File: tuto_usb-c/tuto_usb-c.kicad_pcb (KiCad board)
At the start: 4 copper layers, 50 x 40 mm, 38 parts, among them J1 USB_C_Receptacle_USB2.0, J2 Conn_01x06, J301 Conn_ST_STDC14, J4 Conn_01x06, U1 USBLC6-2SC6, U2 MCP1802x-xx02xOT, U3 STM32G431KBT6, Y1 Crystal_GND24_Small

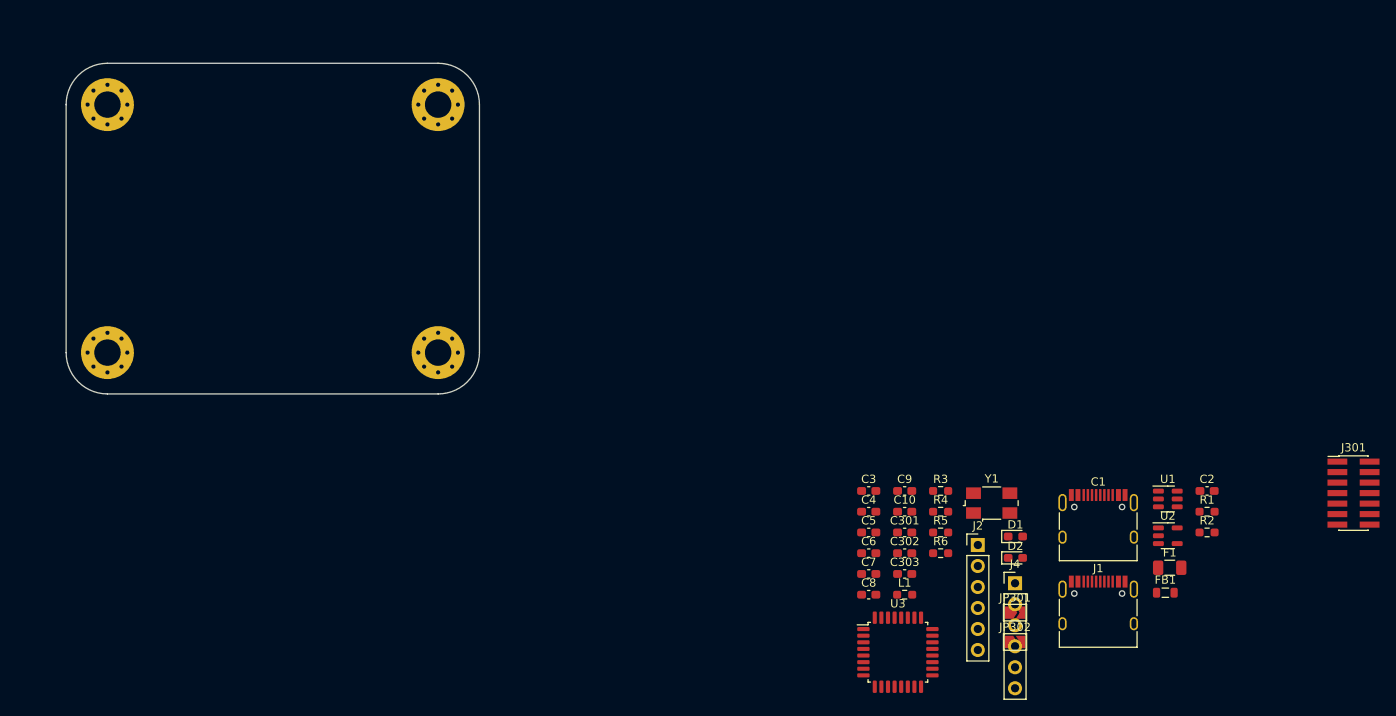
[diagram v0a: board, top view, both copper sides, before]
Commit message: modif routing - add gng plane
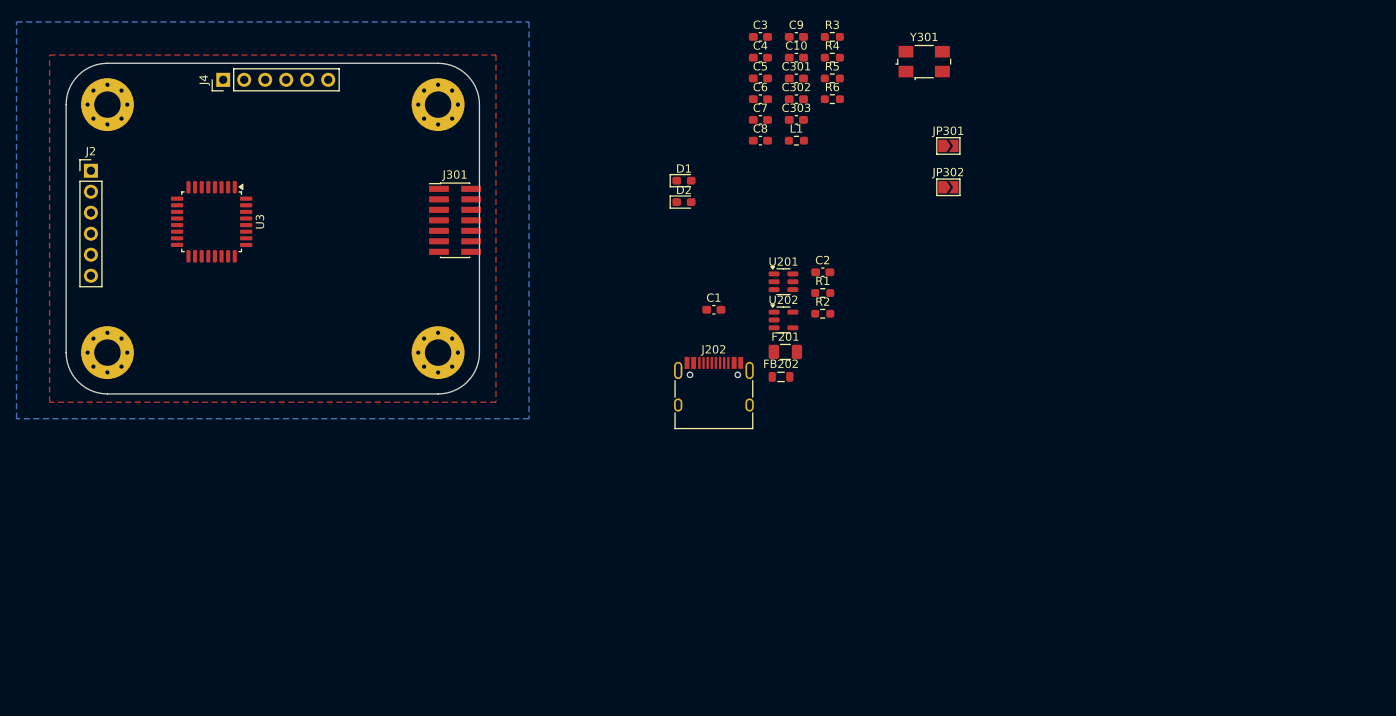
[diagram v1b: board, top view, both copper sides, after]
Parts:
- removed F1: 250mA, Fuse:Fuse_1206_3216Metric
- removed FB1: 600 @ 100MHz, Inductor_SMD:L_0805_2012Metric
- removed J1: USB_C_Receptacle_USB2.0, Connector_USB:USB_C_Receptacle_HRO_TYPE-C-31-M-12
- removed U1: USBLC6-2SC6, Package_TO_SOT_SMD:SOT-23-6
- removed U2: MCP1802x-xx02xOT, Package_TO_SOT_SMD:SOT-23-5
- removed Y1: Crystal_GND24_Small, Crystal:Crystal_SMD_0603-4Pin_6.0x3.5mm
- added F201: 250mA, Fuse:Fuse_1206_3216Metric, F.Cu at (182.0, 79.9)
- added FB202: 600 @ 100MHz, Inductor_SMD:L_0805_2012Metric, F.Cu at (181.5, 82.9)
- added J202: USB_C_Receptacle_USB2.0_16P, Connector_USB:USB_C_Receptacle_HRO_TYPE-C-31-M-12, F.Cu at (173.4, 85.3)
- added U201: USBLC6-2SC6, Package_TO_SOT_SMD:SOT-23-6, F.Cu at (181.8, 71.4)
- added U202: MCP1802x-xx02xOT, Package_TO_SOT_SMD:SOT-23-5, F.Cu at (181.8, 76.0)
- added Y301: Crystal_GND24_Small, Crystal:Crystal_SMD_0603-4Pin_6.0x3.5mm, F.Cu at (198.8, 44.8)
- C1: footprint Connector_USB:USB_C_Receptacle_HRO_TYPE-C-31-M-12 -> Capacitor_SMD:C_0603_1608Metric_Pad1.08x0.95mm_HandSolder
- moved J2 116.5 mm to (98.0, 58.0)
- moved J301 113.6 mm to (142.1, 64.0)
- moved J4 113.5 mm to (114.0, 47.0), turned to 90 degrees
- moved U3 98.0 mm to (112.6, 64.2), turned to -90 degrees
- moved D1 58.8 mm to (169.7, 59.2)
- moved D2 58.8 mm to (169.7, 61.8)
- moved JP301 57.0 mm to (201.7, 55.0)
- moved C10 56.5 mm to (183.3, 44.3)
- moved C303 56.5 mm to (183.3, 51.9)
- moved C4 56.5 mm to (179.0, 44.3)
- moved C7 56.5 mm to (179.0, 51.9)
- moved R4 56.5 mm to (187.7, 44.3)
- moved C3 56.5 mm to (179.0, 41.8)
- moved C301 56.5 mm to (183.3, 46.8)
- moved C302 56.5 mm to (183.3, 49.3)
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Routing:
- added copper zone on In2.Cu, net +3.3V
- added copper zone on B.Cu, net GND
- added copper zone on F.Cu, net GND
- added copper zone on In1.Cu, net GND

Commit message: placement des composants sur la  PCB
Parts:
- Y301: footprint Crystal:Crystal_SMD_0603-4Pin_6.0x3.5mm -> Crystal:Crystal_SMD_EuroQuartz_MT-4Pin_3.2x2.5mm
- moved Y301 97.7 mm to (102.8, 63.4), turned to 90 degrees
- moved JP302 87.9 mm to (114.7, 47.7)
- moved JP301 87.1 mm to (114.7, 51.6), turned to 180 degrees
- moved R4 83.8 mm to (106.3, 64.5)
- moved C5 78.6 mm to (102.8, 66.2), turned to 180 degrees
- moved R6 78.0 mm to (109.9, 54.6), turned to 90 degrees
- moved C4 77.9 mm to (102.8, 60.6), turned to 180 degrees
- moved C9 76.3 mm to (107.4, 49.6), turned to 90 degrees
- moved R5 76.0 mm to (112.1, 54.6), turned to 90 degrees
- moved C10 74.5 mm to (109.0, 49.6), turned to 90 degrees
- moved R3 73.8 mm to (116.8, 62.1), turned to 180 degrees
- moved C301 73.5 mm to (112.4, 66.0), turned to 180 degrees
- moved C8 73.3 mm to (105.8, 49.6), turned to 90 degrees
- moved C302 72.5 mm to (112.4, 64.4), turned to 180 degrees
- moved C3 71.3 mm to (112.8, 68.4), turned to 180 degrees
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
